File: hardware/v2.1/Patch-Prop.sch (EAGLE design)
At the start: 51 parts, among them IC2 ATMEGA168, IC3 MCP1253, IC5 MMA8452Q, IC6 W2RV005RM, IC7 MCP73831

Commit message: Switch for charging topology, added jumper for FTDI, Stepup to V+
-Added a header for a switch between battery and V+. When the switch is
off, only the charger IC is still connected to the battery
-Disconnected FTDI from +3v3 now jumper to V+
-Now connected setupup to V+ instead of +3v3
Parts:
- added SJ4: SOLDERJUMPERNO, SparkFun:SOLDERJUMPERNO
- added SWITCH: (no value), SparkFun:M02PTH
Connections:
- new net N$13: FTDI.VCC, SJ4.1
- new net VBATT: BATT.1, C2.1, IC7.VBAT, SWITCH.2
- net +3V3: no longer C8.1, FTDI.VCC, IC3./SHDN, IC3.VIN
- net V+: now also C8.1, IC3./SHDN, IC3.VIN, SJ4.2, SWITCH.1; no longer BATT.1, C2.1, IC7.VBAT
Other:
- moved on the sheet: BATT, C10, C8, C9, IC3, L1, R6

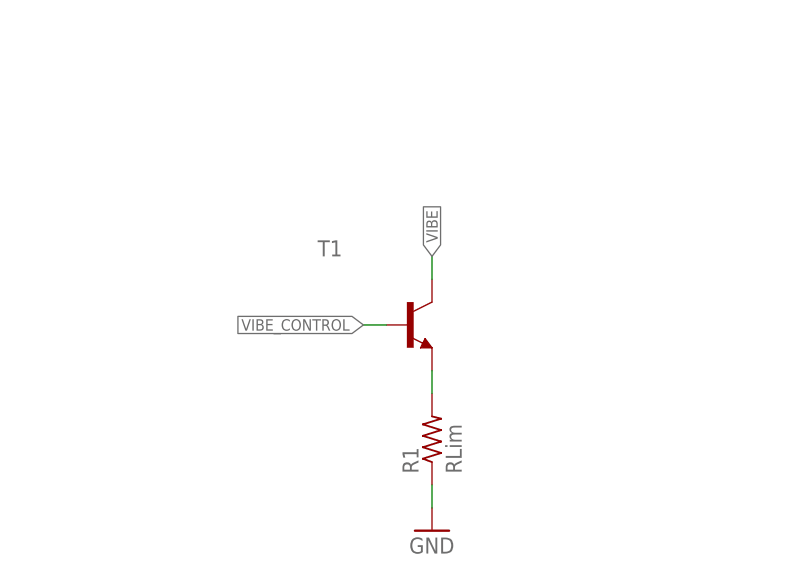
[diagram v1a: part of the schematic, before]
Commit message: Flipped transistor footprint
Flipped to the more common BCE/DGS layout
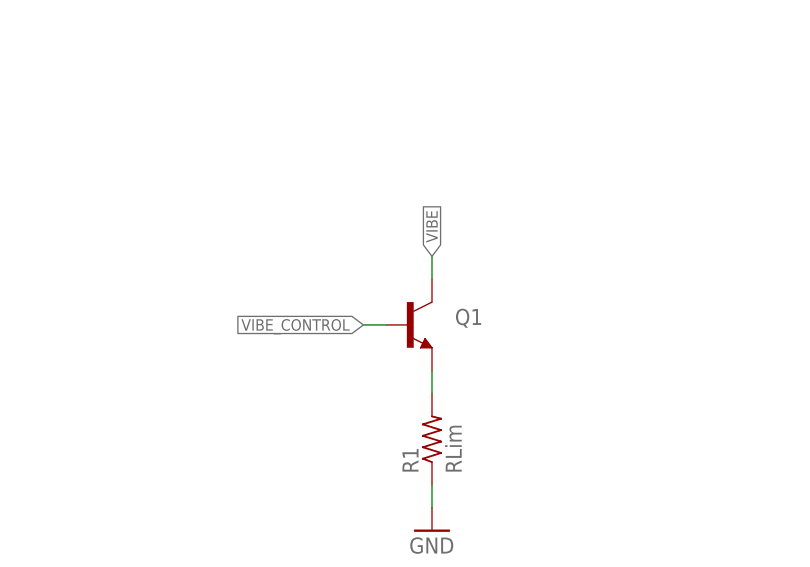
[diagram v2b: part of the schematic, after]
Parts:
- removed T1: (no value), transistor:-NPN-SOT23-EBC
- added Q1: (no value), SparkFun:TRANSISTOR_NPNSOT23
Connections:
- net N$4: now also Q1.E; no longer T1.E
- net VIBE: now also Q1.C; no longer T1.C
- net VIBE_CONTROL: now also Q1.B; no longer T1.B
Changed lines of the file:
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@@
 <part name="LED5" library="adafruit" deviceset="RGBLED" device="5050"/>
 <part name="SJ2" library="SparkFun" deviceset="SOLDERJUMPER" device="NO"/>
-<part name="T1" library="transistor" deviceset="*-NPN-" device="SOT23-EBC"/>
 <part name="GND11" library="supply1" deviceset="GND" device=""/>
 <part name="PWR" library="led" deviceset="LED" device="CHIPLED_0805"/>
@@
 <part name="SJ4" library="SparkFun" deviceset="SOLDERJUMPER" device="NO"/>
 <part name="SUPPLY3" library="supply2" deviceset="V+" device=""/>
+<part name="Q1" library="SparkFun" deviceset="TRANSISTOR_NPN" device="SOT23"/>
 </parts>
 <sheets>
@@
 <instance part="LED5" gate="G$1" x="411.48" y="45.72"/>
 <instance part="SJ2" gate="1" x="424.18" y="350.52" rot="R180"/>
-<instance part="T1" gate="G$1" x="86.36" y="96.52"/>
 <instance part="GND11" gate="1" x="218.44" y="332.74"/>
 <instance part="PWR" gate="G$1" x="259.08" y="210.82"/>
@@
 <instance part="SJ4" gate="1" x="297.18" y="218.44" rot="R180"/>
 <instance part="SUPPLY3" gate="1" x="284.48" y="218.44" rot="R90"/>
+<instance part="Q1" gate="G$1" x="86.36" y="96.52"/>
 </instances>
 <busses>
@@
 <net name="VIBE_CONTROL" class="0">
 <segment>
-<pinref part="T1" gate="G$1" pin="B"/>
+<label x="81.28" y="96.52" size="1.27" layer="95" font="vector" ratio="15" rot="R180" xref="yes"/>
+<pinref part="Q1" gate="G$1" pin="B"/>
 <wire x1="83.82" y1="96.52" x2="81.28" y2="96.52" width="0.1524" layer="91"/>
-<label x="81.28" y="96.52" size="1.27" layer="95" font="vector" ratio="15" rot="R180" xref="yes"/>
 </segment>
 <segment>
@@
 <net name="VIBE" class="0">
 <segment>
-<pinref part="T1" gate="G$1" pin="C"/>
+<label x="88.9" y="104.14" size="1.27" layer="95" font="vector" ratio="15" rot="R90" xref="yes"/>
+<pinref part="Q1" gate="G$1" pin="C"/>
 <wire x1="88.9" y1="101.6" x2="88.9" y2="104.14" width="0.1524" layer="91"/>
-<label x="88.9" y="104.14" size="1.27" layer="95" font="vector" ratio="15" rot="R90" xref="yes"/>
 </segment>
 <segment>
@@
 <net name="N$4" class="0">
 <segment>
-<pinref part="T1" gate="G$1" pin="E"/>
 <pinref part="R1" gate="G$1" pin="2"/>
+<pinref part="Q1" gate="G$1" pin="E"/>
 <wire x1="88.9" y1="91.44" x2="88.9" y2="88.9" width="0.1524" layer="91"/>
 </segment>
